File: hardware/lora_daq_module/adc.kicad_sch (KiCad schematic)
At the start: 9 parts, among them J1 JST3pinfemale, U1 OPA333, U2 ADS1115IDGS

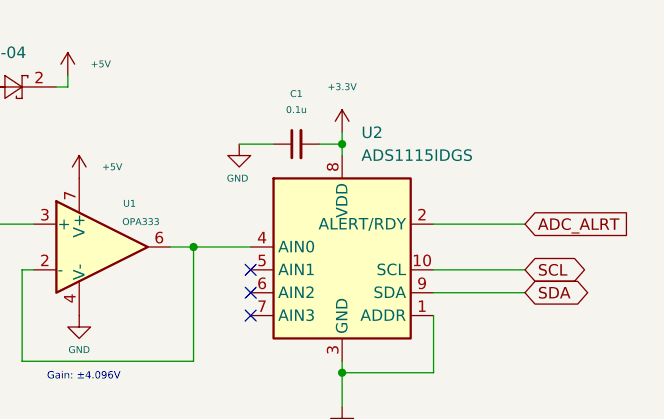
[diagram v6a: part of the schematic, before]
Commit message: assign parts and update BOM in symbol field table, warn: pcb footprints need update
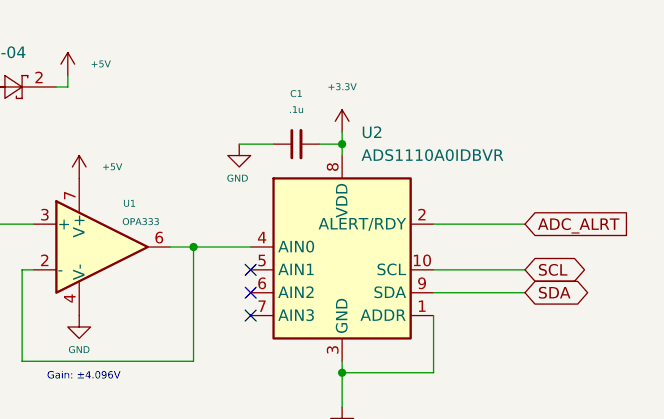
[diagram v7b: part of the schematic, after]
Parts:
- C1: value 0.1u -> .1u; Desc (none) -> CAP CER 0.1UF 16V X7R 0603; Dist (none) -> Digikey; Dist PN (none) -> 311-1088-1-ND; Mfr (none) -> YAGEO; Mfr PN (none) -> CC0603KRX7R7BB104
- C2: Desc (none) -> CAP CER 0.047UF 25V X7R 0603; Dist (none) -> Digikey; Dist PN (none) -> 311-1373-1-ND; Mfr (none) -> YAGEO; Mfr PN (none) -> CC0603KRX7R8BB473
- D7: Desc (none) -> Diode Array 1 Pair Series Connection 40 V 200mA Surface Mou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; Dist (none) -> Digikey; Dist PN (none) -> 4878-BAS40-04CT-ND; Mfr (none) -> Diotec Semiconductor; Mfr PN (none) -> BAS40-04
- J1: Desc (none) -> Connector Header Through Hole 3 position 0.098" (2.50mm); Dist (none) -> Digikey; Dist PN (none) -> 455-B3B-EH-A-ND; Mfr (none) -> JST Sales America Inc.; Mfr PN (none) -> B3B-EH-A
- R1: Desc (none) -> 47 kOhms ±1% 0.1W, 1/10W Chip Resistor 0603 (1608 Metric) M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; Dist (none) -> Digikey; Dist PN (none) -> 311-47.0KHRCT-ND; Mfr (none) -> YAGEO; Mfr PN (none) -> RC0603FR-0747KL
- R2: Desc (none) -> 220 kOhms ±1% 0.1W, 1/10W Chip Resistor 0603 (1608 Metric) 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; Dist (none) -> Digikey; Dist PN (none) -> RMCF0603FT220KCT-ND; Mfr (none) -> Stackpole Electronics Inc; Mfr PN (none) -> RES 220K OHM 1% 1/10W 0603
- R3: Desc (none) -> 1 kOhms ±1% 0.1W, 1/10W Chip Resistor 0603 (1608 Metric) Au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; Dist (none) -> Digikey; Dist PN (none) -> RMCF0603FT1K00CT-ND; Mfr (none) -> Stackpole Electronics Inc; Mfr PN (none) -> RMCF0603FT1K00
- U1: footprint Package_SO:SOIC-8_3.9x4.9mm_P1.27mm -> Package_TO_SOT_SMD:SOT-353_SC-70-5_Handsoldering; Desc (none) -> IC OPAMP ZERO-DRIFT 1CIRC SC70-5; Dist (none) -> Digikey; Dist PN (none) -> 296-19547-1-ND; Mfr (none) -> Texas Instruments; Mfr PN (none) -> OPA333AIDCKR
- U2: value ADS1115IDGS -> ADS1110A0IDBVR; footprint Package_SO:TSSOP-10_3x3mm_P0.5mm -> Package_TO_SOT_SMD:SOT-23-6_Handsoldering; Desc (none) -> IC ADC 16BIT SIGMA-DELTA SOT23-6; Dist (none) -> Digikey; Dist PN (none) -> 296-25890-1-ND; Mfr (none) -> Texas Instruments; Mfr PN (none) -> ADS1110A0IDBVR
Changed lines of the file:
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@@
 			)
 		)
-		(property "Desc" ""
+		(property "Desc" "220 kOhms ±1% 0.1W, 1/10W Chip Resistor 0603 (1608 Metric) Automotive AEC-Q200 Thick Film"
 			(at 125.73 105.41 0)
 			(effects
@@
 			)
 		)
-		(property "Dist" ""
+		(property "Dist" "Digikey"
 			(at 125.73 105.41 0)
 			(effects
@@
 			)
 		)
-		(property "Dist PN" ""
+		(property "Dist PN" "RMCF0603FT220KCT-ND"
 			(at 125.73 105.41 0)
 			(effects
@@
 			)
 		)
-		(property "Mfr" ""
+		(property "Mfr" "Stackpole Electronics Inc"
 			(at 125.73 105.41 0)
 			(effects
@@
 			)
 		)
-		(property "Mfr PN" ""
+		(property "Mfr PN" "RES 220K OHM 1% 1/10W 0603"
 			(at 125.73 105.41 0)
 			(effects
@@
 			)
 		)
-		(property "Desc" ""
+		(property "Desc" "CAP CER 0.047UF 25V X7R 0603"
 			(at 138.43 105.41 0)
 			(effects
@@
 			)
 		)
-		(property "Dist" ""
+		(property "Dist" "Digikey"
 			(at 138.43 105.41 0)
 			(effects
@@
 			)
 		)
-		(property "Dist PN" ""
+		(property "Dist PN" "311-1373-1-ND"
 			(at 138.43 105.41 0)
 			(effects
@@
 			)
 		)
-		(property "Mfr" ""
+		(property "Mfr" "YAGEO"
 			(at 138.43 105.41 0)
 			(effects
@@
 			)
 		)
-		(property "Mfr PN" ""
+		(property "Mfr PN" "CC0603KRX7R8BB473"
 			(at 138.43 105.41 0)
 			(effects
@@
 			)
 		)
-		(property "Desc" ""
+		(property "Desc" "Diode Array 1 Pair Series Connection 40 V 200mA Surface Mount TO-236-3, SC-59, SOT-23-3"
 			(at 147.32 88.9 0)
 			(effects
@@
 			)
 		)
-		(property "Dist" ""
+		(property "Dist" "Digikey"
 			(at 147.32 88.9 0)
 			(effects
@@
 			)
 		)
-		(property "Dist PN" ""
+		(property "Dist PN" "4878-BAS40-04CT-ND"
 			(at 147.32 88.9 0)
 			(effects
@@
 			)
 		)
-		(property "Mfr" ""
+		(property "Mfr" "Diotec Semiconductor"
 			(at 147.32 88.9 0)
 			(effects
@@
 			)
 		)
-		(property "Mfr PN" ""
+		(property "Mfr PN" "BAS40-04"
 			(at 147.32 88.9 0)
 			(effects
@@
 			)
 		)
-		(property "Desc" ""
+		(property "Desc" "47 kOhms ±1% 0.1W, 1/10W Chip Resistor 0603 (1608 Metric) Moisture Resistant Thick Film"
 			(at 121.92 101.6 90)
 			(effects
@@
 			)
 		)
-		(property "Dist" ""
+		(property "Dist" "Digikey"
 			(at 121.92 101.6 90)
 			(effects
@@
 			)
 		)
-		(property "Dist PN" ""
+		(property "Dist PN" "311-47.0KHRCT-ND"
 			(at 121.92 101.6 90)
 			(effects
@@
 			)
 		)
-		(property "Mfr" ""
+		(property "Mfr" "YAGEO"
 			(at 121.92 101.6 90)
 			(effects
@@
 			)
 		)
-		(property "Mfr PN" ""
+		(property "Mfr PN" "RC0603FR-0747KL"
 			(at 121.92 101.6 90)
 			(effects
@@
 			)
 		)
-		(property "Desc" ""
+		(property "Desc" "1 kOhms ±1% 0.1W, 1/10W Chip Resistor 0603 (1608 Metric) Automotive AEC-Q200 Thick Film"
 			(at 134.62 105.41 0)
 			(effects
@@
 			)
 		)
-		(property "Dist" ""
+		(property "Dist" "Digikey"
 			(at 134.62 105.41 0)
 			(effects
@@
 			)
 		)
-		(property "Dist PN" ""
+		(property "Dist PN" "RMCF0603FT1K00CT-ND"
 			(at 134.62 105.41 0)
 			(effects
@@
 			)
 		)
-		(property "Mfr" ""
+		(property "Mfr" "Stackpole Electronics Inc"
 			(at 134.62 105.41 0)
 			(effects
@@
 			)
 		)
-		(property "Mfr PN" ""
+		(property "Mfr PN" "RMCF0603FT1K00"
 			(at 134.62 105.41 0)
 			(effects
@@
 			)
 		)
-		(property "Value" "0.1u"
+		(property "Value" ".1u"
 			(at 181.6163 88.9 90)
 			(effects
@@
 			)
 		)
-		(property "Desc" ""
+		(property "Desc" "CAP CER 0.1UF 16V X7R 0603"
 			(at 181.61 92.71 90)
 			(effects
@@
 			)
 		)
-		(property "Dist" ""
+		(property "Dist" "Digikey"
 			(at 181.61 92.71 90)
 			(effects
@@
 			)
 		)
-		(property "Dist PN" ""
+		(property "Dist PN" "311-1088-1-ND"
 			(at 181.61 92.71 90)
 			(effects
@@
 			)
 		)
-		(property "Mfr" ""
+		(property "Mfr" "YAGEO"
 			(at 181.61 92.71 90)
 			(effects
@@
 			)
 		)
-		(property "Mfr PN" ""
+		(property "Mfr PN" "CC0603KRX7R7BB104"
 			(at 181.61 92.71 90)
 			(effects
@@
 			)
 		)
-		(property "Footprint" "Package_SO:SOIC-8_3.9x4.9mm_P1.27mm"
+		(property "Footprint" "Package_TO_SOT_SMD:SOT-353_SC-70-5_Handsoldering"
 			(at 157.48 109.22 0)
 			(effects
@@
 			)
 		)
-		(property "Desc" ""
+		(property "Desc" "IC OPAMP ZERO-DRIFT 1CIRC SC70-5"
 			(at 160.02 104.14 0)
 			(effects
@@
 			)
 		)
-		(property "Dist" ""
+		(property "Dist" "Digikey"
 			(at 160.02 104.14 0)
 			(effects
@@
 			)
 		)
-		(property "Dist PN" ""
+		(property "Dist PN" "296-19547-1-ND"
 			(at 160.02 104.14 0)
 			(effects
@@
 			)
 		)
-		(property "Mfr" ""
+		(property "Mfr" "Texas Instruments"
 			(at 160.02 104.14 0)
 			(effects
@@
 			)
 		)
-		(property "Mfr PN" ""
+		(property "Mfr PN" "OPA333AIDCKR"
 			(at 160.02 104.14 0)
 			(effects
@@
 			)
 		)
-		(property "Desc" ""
+		(property "Desc" "Connector Header Through Hole 3 position 0.098\" (2.50mm)"
 			(at 95.25 104.14 0)
 			(effects
@@
 			)
 		)
-		(property "Dist" ""
+		(property "Dist" "Digikey"
 			(at 95.25 104.14 0)
 			(effects
@@
 			)
 		)
-		(property "Dist PN" ""
+		(property "Dist PN" "455-B3B-EH-A-ND"
 			(at 95.25 104.14 0)
 			(effects
@@
 			)
 		)
-		(property "Mfr" ""
+		(property "Mfr" "JST Sales America Inc."
 			(at 95.25 104.14 0)
 			(effects
@@
 			)
 		)
-		(property "Mfr PN" ""
+		(property "Mfr PN" "B3B-EH-A"
 			(at 95.25 104.14 0)
 			(effects
@@
 			)
 		)
-		(property "Value" "ADS1115IDGS"
+		(property "Value" "ADS1110A0IDBVR"
 			(at 188.8333 93.98 0)
 			(effects
@@
 			)
 		)
-		(property "Footprint" "Package_SO:TSSOP-10_3x3mm_P0.5mm"
+		(property "Footprint" "Package_TO_SOT_SMD:SOT-23-6_Handsoldering"
 			(at 186.69 119.38 0)
 			(effects
@@
 			)
 		)
-		(property "Desc" ""
+		(property "Desc" "IC ADC 16BIT SIGMA-DELTA SOT23-6"
 			(at 186.69 106.68 0)
 			(effects
@@
 			)
 		)
-		(property "Dist" ""
+		(property "Dist" "Digikey"
 			(at 186.69 106.68 0)
 			(effects
@@
 			)
 		)
-		(property "Dist PN" ""
+		(property "Dist PN" "296-25890-1-ND"
 			(at 186.69 106.68 0)
 			(effects
@@
 			)
 		)
-		(property "Mfr" ""
+		(property "Mfr" "Texas Instruments"
 			(at 186.69 106.68 0)
 			(effects
@@
 			)
 		)
-		(property "Mfr PN" ""
+		(property "Mfr PN" "ADS1110A0IDBVR"
 			(at 186.69 106.68 0)
 			(effects

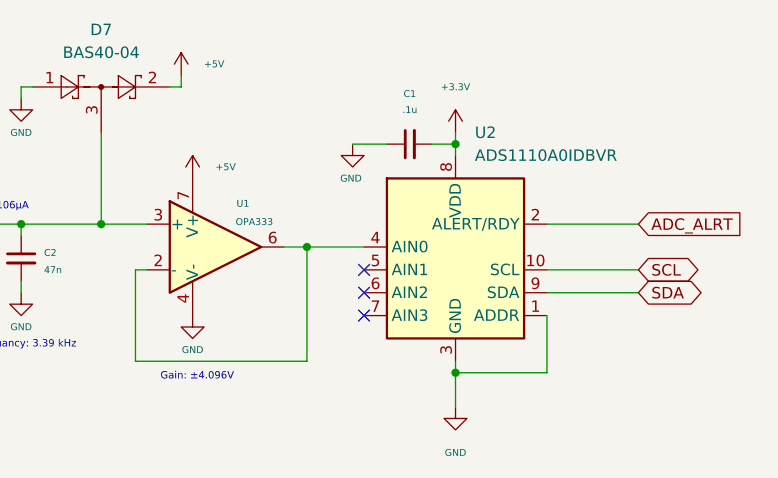
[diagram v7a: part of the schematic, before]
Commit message: lay traces to all components
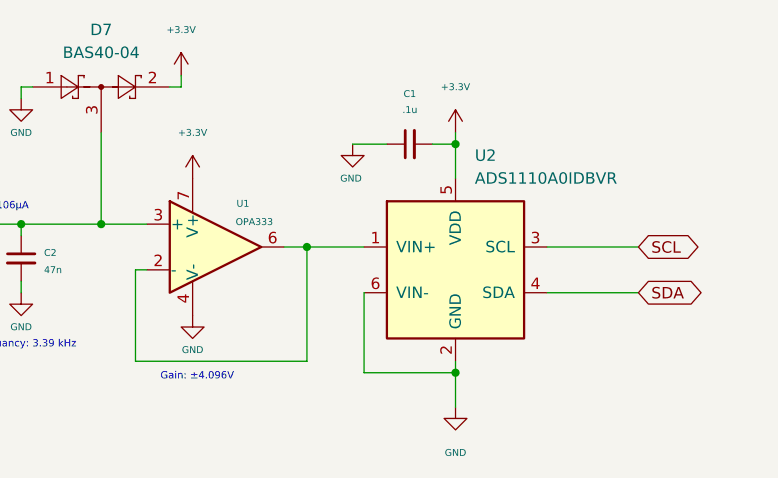
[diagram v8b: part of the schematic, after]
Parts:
- U2: footprint Package_TO_SOT_SMD:SOT-23-6_Handsoldering -> Package_TO_SOT_SMD:SOT-23-6; symbol Analog_ADC:ADS1115IDGS -> Analog_ADC:ADS1110
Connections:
- net +5V is gone; now on net +3.3V: D7.2, U1.7 (V+)
- net ADC_ALRT is gone; now on net GND: U2.2 (GND)
- net +3.3V: now also U2.5 (VDD); no longer U2.8 (VDD)
- net GND: now also U2.6 (VIN-); no longer U2.1 (ADDR), U2.3 (GND)
- net SCL: now also U2.3 (SCL); no longer U2.10 (SCL)
- net SDA: now also U2.4 (SDA); no longer U2.9 (SDA)
- net at U1.2 (-), U1.6: now also U2.1 (VIN+); no longer U2.4 (AIN0)
- no-connect marks 3 -> 0
